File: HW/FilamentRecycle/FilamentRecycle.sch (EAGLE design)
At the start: 55 parts, among them CON5 MOLEX-53261-0671, IC1 ATMEGA48A-AU, IC2 74HC595D, IC7 FT232RL, Q1 16MHz, Q2 BC847ALT1SMD, Q3 BC847ALT1SMD, X6 PN61729-S

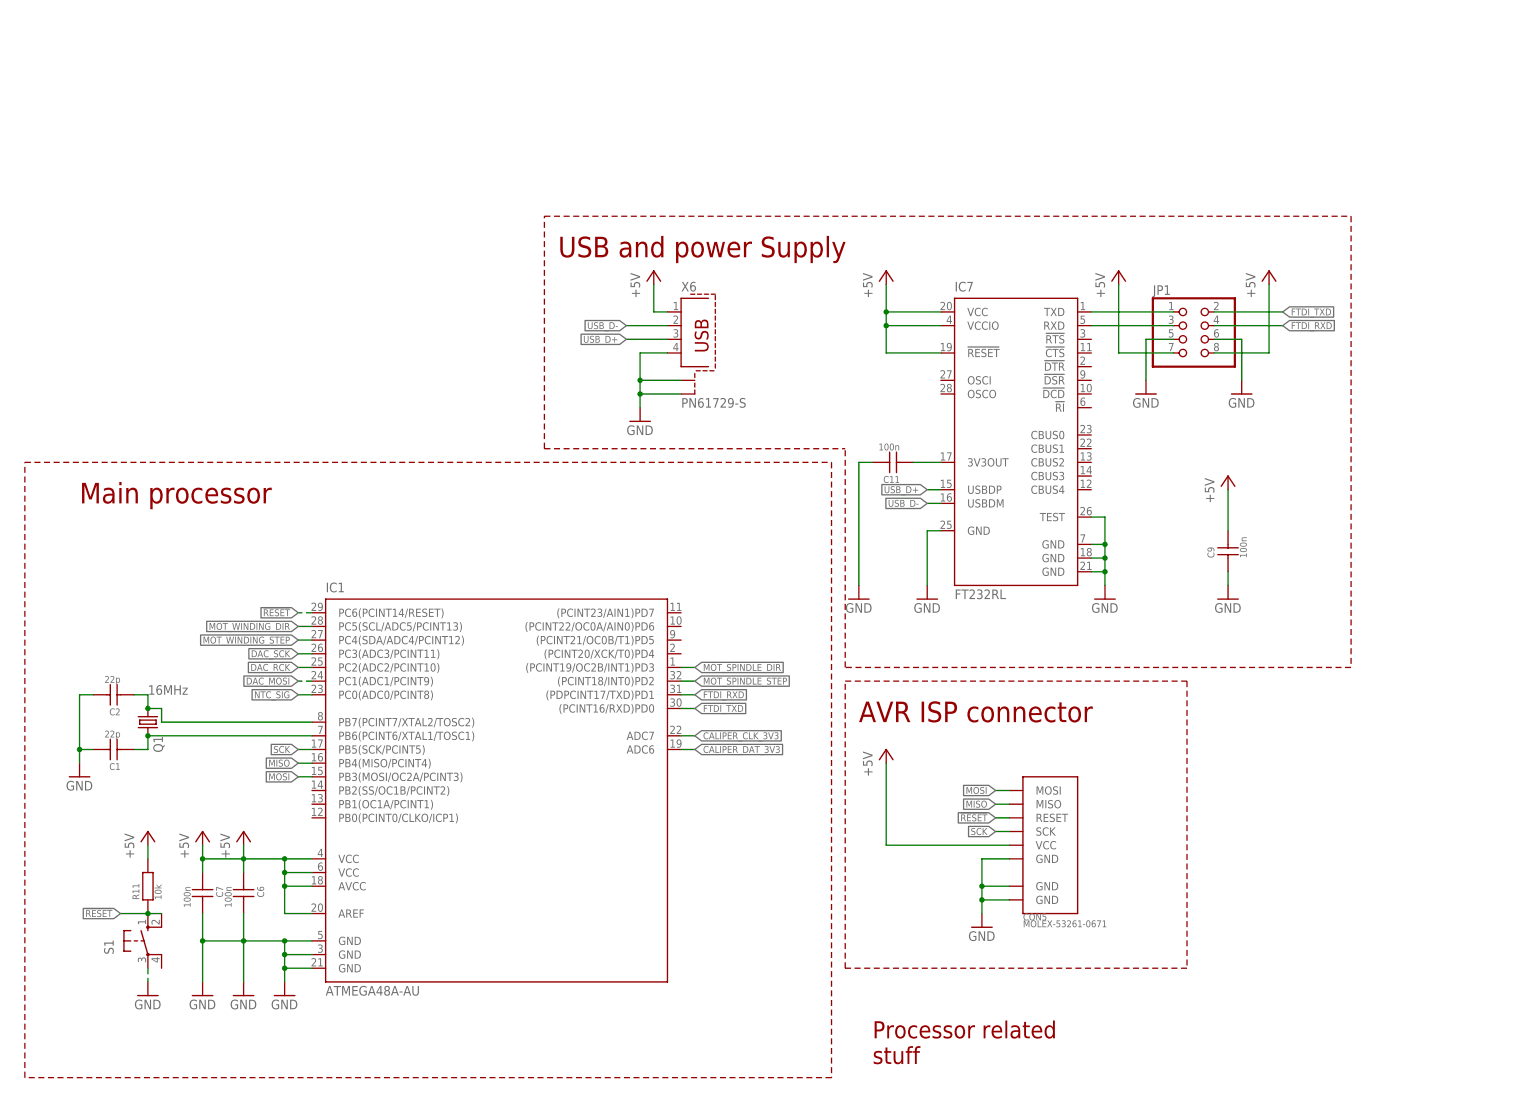
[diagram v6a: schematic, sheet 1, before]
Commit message: First tests of target hardware. DAC, Caliper and thermistor working
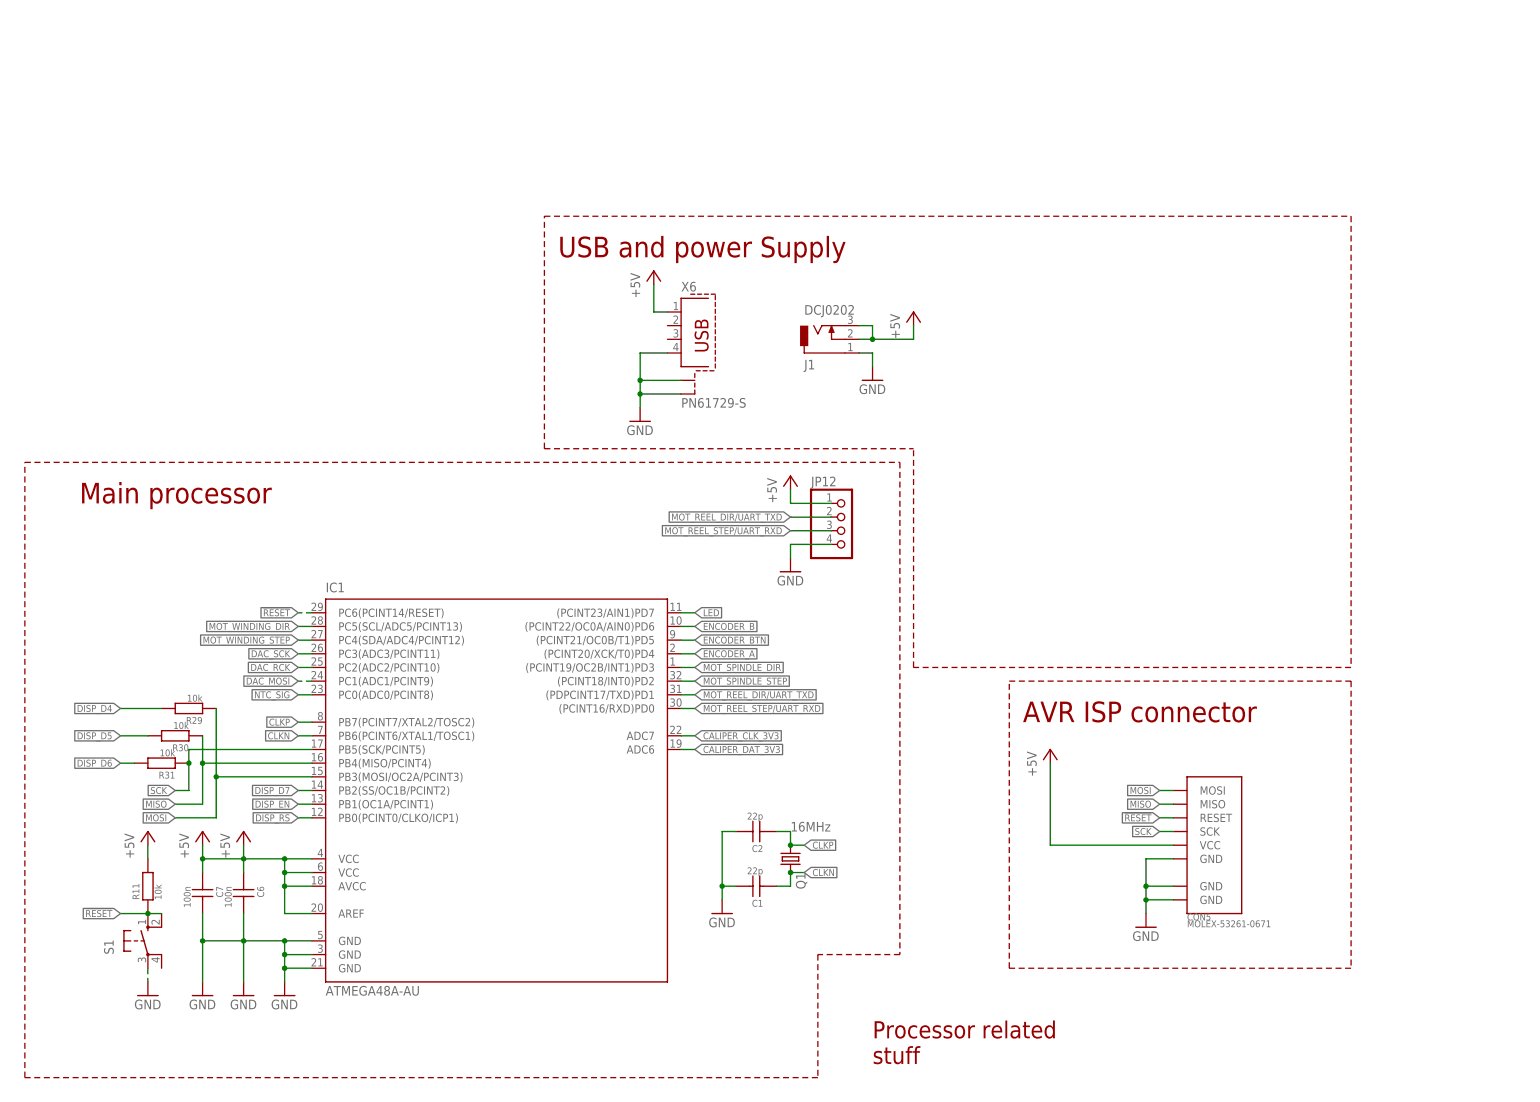
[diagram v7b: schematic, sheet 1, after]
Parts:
- removed C11, C9: 100n, SchlegelAr_Master:C_SMD0603
- removed IC7: FT232RL, SchlegelAr_Master:FT232RL
- added J1: DCJ0202, con-jack:DCJ0202
- added JP11, JP12: (no value), pinhead:PINHD-1X4
- added R29, R30, R31: 10k, SchlegelAr_Master:R0603
- added R32: 10k, rcl:R-EU_R0603
- added R33: 100k, rcl:R-EU_R0603
- added SV2, SV3: (no value), con-harting-ml:ML10
- added U$9: A4988BREAKOUT, RepRapjr:A4988BREAKOUT
- JP1: device pinhead:PINHD-2X4 -> pinhead:PINHD-2X3
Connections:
- net N$1 renamed CLKP
- net N$2 renamed CLKN
- removed net FTDI_3V3OUT: C11.P$1, IC7.3V3OUT
- removed net FTDI_RXD: IC1.(PDPCINT17/TXD)PD1, JP1.4
- removed net FTDI_TXD: IC1.(PCINT16/RXD)PD0, JP1.2
- removed net USB_D+: IC7.USBDP, X6.3
- removed net USB_D-: IC7.USBDM, X6.2
- new net !MOT_WINDING_EN1: R32.2, U$9.EN
- new net DISP_D4: R29.P$2, SV3.7
- new net DISP_D5: R30.P$2, SV3.5
- new net DISP_D6: R31.P$2, SV3.3
- new net DISP_D7: IC1.PB2(SS/OC1B/PCINT2), SV3.1
- new net DISP_EN: IC1.PB1(OC1A/PCINT1), SV3.6
- new net DISP_RS: IC1.PB0(PCINT0/CLKO/ICP1), SV3.8
- new net ENCODER_A: IC1.(PCINT20/XCK/T0)PD4, SV2.8
- new net ENCODER_B: IC1.(PCINT22/OC0A/AIN0)PD6, SV2.4
- new net ENCODER_BTN: IC1.(PCINT21/OC0B/T1)PD5, SV2.6
- new net LED: IC1.(PCINT23/AIN1)PD7, SV2.7
- new net MOT_REEL_DIR/UART_TXD: IC1.(PDPCINT17/TXD)PD1, JP12.2, U$9.DIR
- new net MOT_REEL_STEP/UART_RXD: IC1.(PCINT16/RXD)PD0, JP12.3, U$9.STEP
- new net N$1: JP1.5, U$9.MS3
- new net N$2: JP1.1, R33.1, U$9.MS1
- new net N$31: JP11.2, U$9.2A
- new net N$40: JP11.3, U$9.1A
- new net N$41: JP11.4, U$9.1B
- new net N$42: U$9.RST, U$9.SLEEP
- net +12V: now also U$9.VMOT
- net +5V: now also J1.2, J1.3, JP1.2, JP1.4, JP1.6, JP12.1, SV2.10, SV3.10, U$9.VDD; no longer C9.P$2, IC7.!RESET, IC7.VCC, IC7.VCCIO, JP1.7, JP1.8
- net GND: now also J1.1, JP12.4, R32.1, R33.2, SV2.2, SV3.2, U$9.GND@0, U$9.GND@1; no longer C11.P$2, C9.P$1, IC7.GND, IC7.GND@1, IC7.GND@2, IC7.GND@A, IC7.TEST, JP1.5, JP1.6
- net MISO: now also R30.P$1
- net MOSI: now also R29.P$1
- net N$5: now also JP1.3, U$9.MS2; no longer IC7.TXD, JP1.1
- net N$8: now also JP11.1, U$9.2B; no longer IC7.RXD, JP1.3
- net SCK: now also R31.P$1
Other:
- moved on the sheet: C1, C2, CON5, Q1

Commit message: Added LCD library, Fixed hw bug (series resistors for LCD removed)
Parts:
- R29, R30, R31: value 10k -> 0R
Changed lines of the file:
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@@
 <part name="P+5" library="supply1" deviceset="+5V" device=""/>
 <part name="GND16" library="supply1" deviceset="GND" device=""/>
-<part name="R29" library="SchlegelAr_Master" deviceset="R" device="0603" value="10k"/>
-<part name="R30" library="SchlegelAr_Master" deviceset="R" device="0603" value="10k"/>
-<part name="R31" library="SchlegelAr_Master" deviceset="R" device="0603" value="10k"/>
+<part name="R29" library="SchlegelAr_Master" deviceset="R" device="0603" value="0R"/>
+<part name="R30" library="SchlegelAr_Master" deviceset="R" device="0603" value="0R"/>
+<part name="R31" library="SchlegelAr_Master" deviceset="R" device="0603" value="0R"/>
 <part name="P+8" library="supply1" deviceset="+12V" device=""/>
 <part name="GND1" library="supply1" deviceset="GND" device=""/>
